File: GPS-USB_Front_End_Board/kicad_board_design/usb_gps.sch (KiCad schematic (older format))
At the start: 1 part, among them P1 CONN_02X12

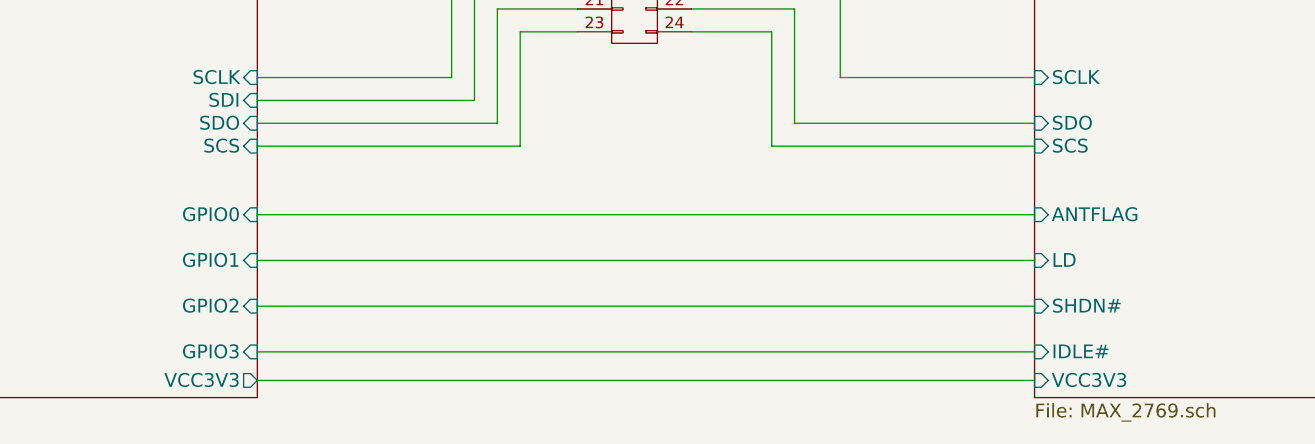
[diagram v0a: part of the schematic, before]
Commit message: Update to MAX2771.  Changes to decoupling caps, Remove ANTFLAG, IDLE signals.  Add explicit antenna bias.  New matching network for LNA input.  Remove bypass for SAW filter.
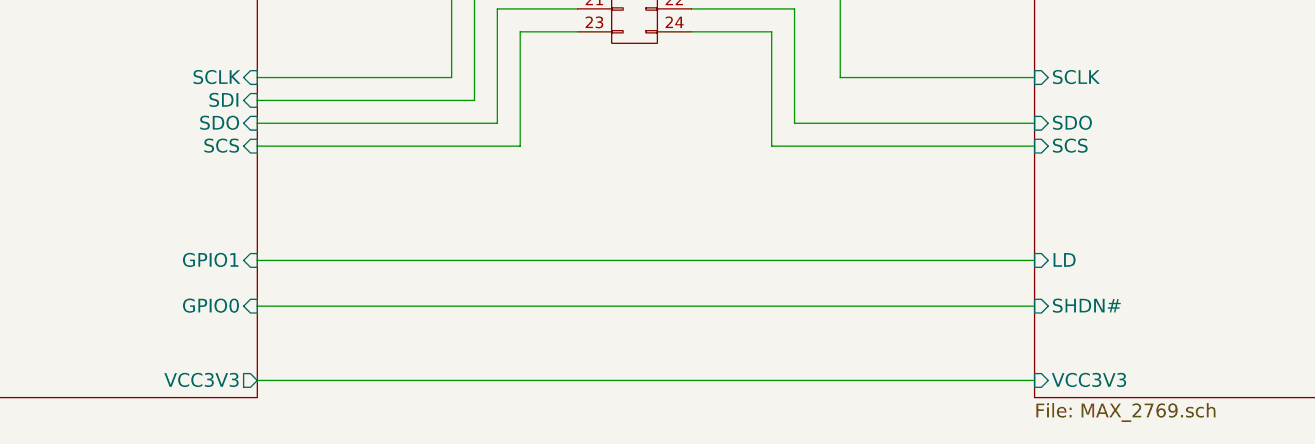
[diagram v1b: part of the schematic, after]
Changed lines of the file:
@@
 F12 "GND" I R 3600 2900 60
 F13 "SDI" I R 3600 4200 60
-F14 "GPIO0" I R 3600 4700 60
-F15 "GPIO1" I R 3600 4900 60
-F16 "GPIO2" I R 3600 5100 60
-F17 "GPIO3" I R 3600 5300 60
-F18 "VCC3V3" O R 3600 5425 60
+F14 "GPIO1" I R 3600 4900 60
+F15 "GPIO0" I R 3600 5100 60
+F16 "VCC3V3" O R 3600 5425 60
 $EndSheet
 $Sheet
@@
 F10 "D3" I L 7000 3400 60
 F11 "SCS" I L 7000 4400 60
-F12 "ANTFLAG" I L 7000 4700 60
-F13 "LD" I L 7000 4900 60
-F14 "SHDN#" I L 7000 5100 60
-F15 "IDLE#" I L 7000 5300 60
-F16 "VCC3V3" I L 7000 5425 60
+F12 "LD" I L 7000 4900 60
+F13 "SHDN#" I L 7000 5100 60
+F14 "VCC3V3" I L 7000 5425 60
 $EndSheet
 $Comp
@@
 	5850 3900 5500 3900
 Wire Wire Line
-	3600 4700 7000 4700
-Wire Wire Line
 	3600 4900 7000 4900
 Wire Wire Line
 	3600 5100 7000 5100
 Wire Wire Line
-	3600 5300 7000 5300
-Wire Wire Line
 	4050 3300 4050 3200

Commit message: Fix value display on EEPROM.  Consolidate some part values.
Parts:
- P1: MFR (none) -> Sullins; MPN (none) -> SFH11-PBPC-D12-ST-BK; SPN (none) -> S9708-ND; SPR (none) -> Digikey
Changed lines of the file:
@@
 F 2 "Pin_Headers:Pin_Header_Straight_2x12" H 5250 2150 50  0001 C CNN
 F 3 "" H 5250 2150 50  0000 C CNN
+F 4 "Sullins" H 5250 3350 60  0001 C CNN "MFR"
+F 5 "SFH11-PBPC-D12-ST-BK" H 5250 3350 60  0001 C CNN "MPN"
+F 6 "Digikey" H 5250 3350 60  0001 C CNN "SPR"
+F 7 "S9708-ND" H 5250 3350 60  0001 C CNN "SPN"
 	1    5250 3350
 	1    0    0    -1
